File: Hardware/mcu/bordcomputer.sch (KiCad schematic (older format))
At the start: 4 parts, among them P101 CONN_1, P102 CONN_1, P103 CONN_1, P104 CONN_1

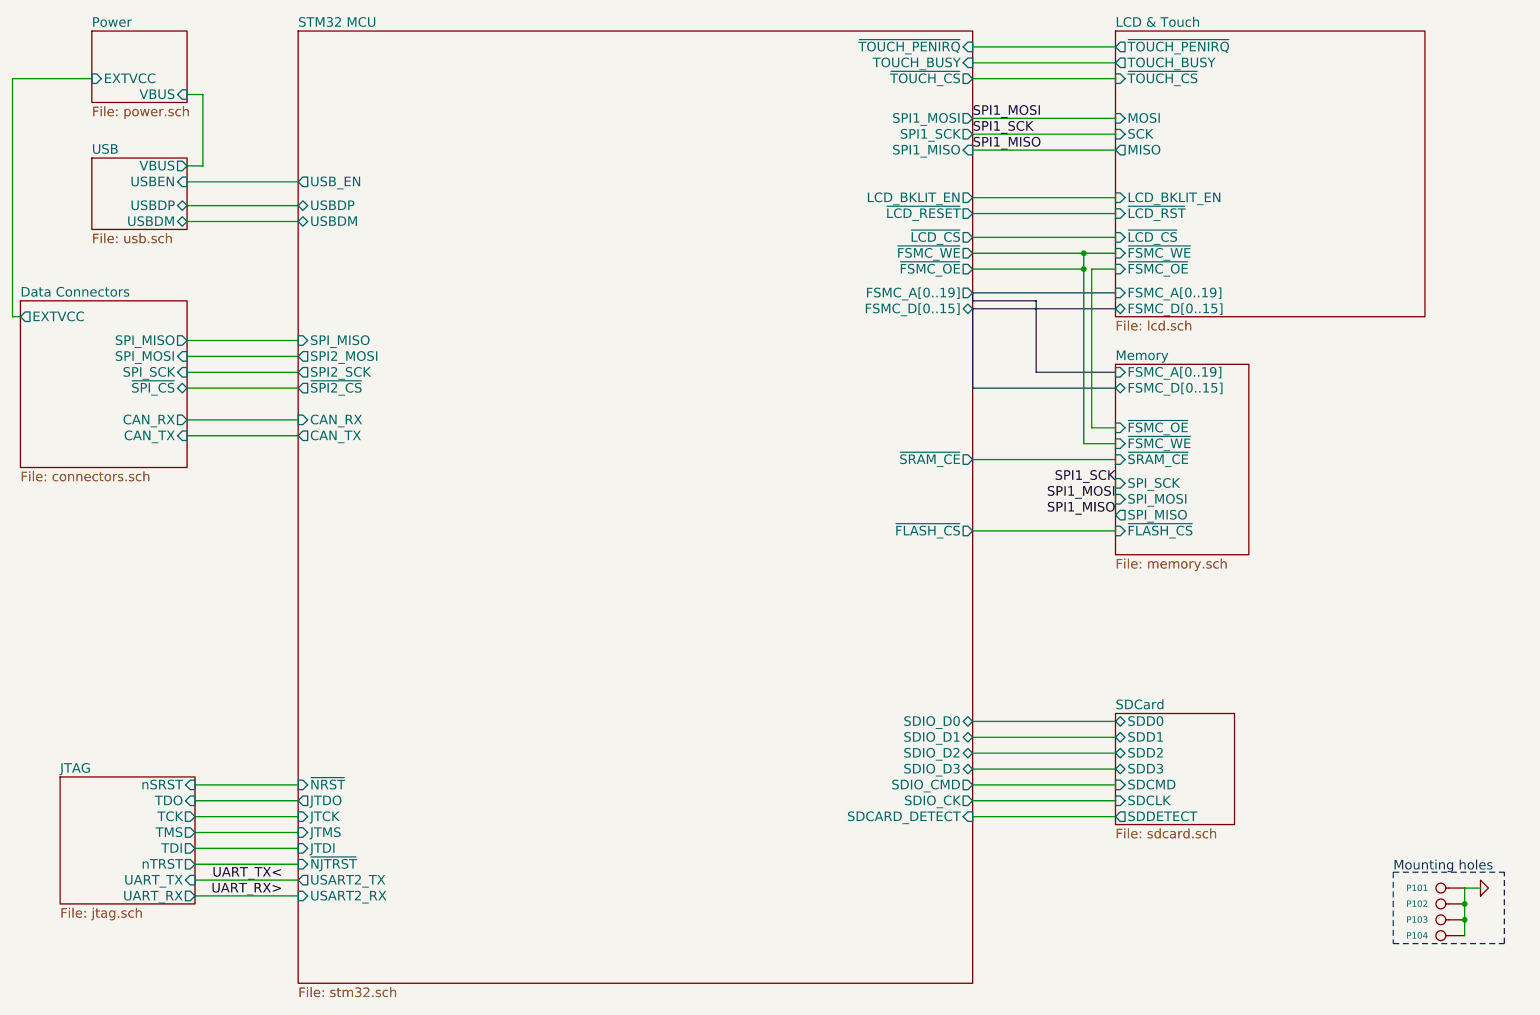
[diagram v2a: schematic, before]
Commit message: using adc instead of analog multiplexer for sensor board, some work on mcu board
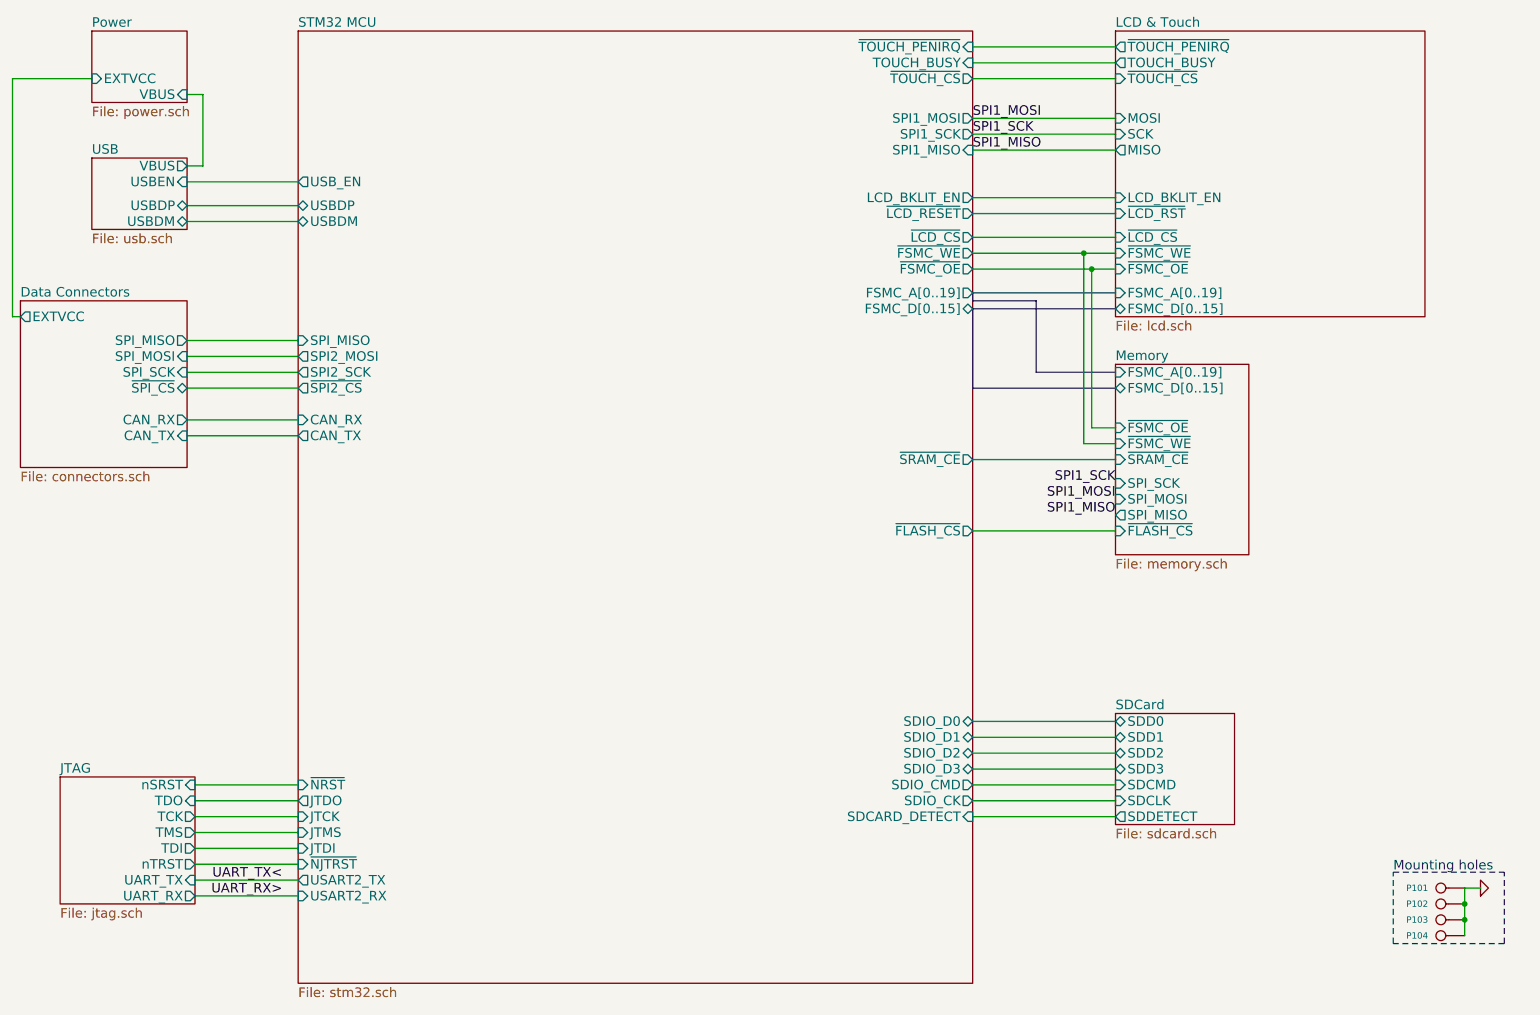
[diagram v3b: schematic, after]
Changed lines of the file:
@@
-EESchema Schematic File Version 2  date Mo 21 Mär 2011 03:16:23 CET
+EESchema Schematic File Version 2  date Di 17 Mai 2011 02:16:23 CEST
 LIBS:power
 LIBS:device
@@
 Sheet 1 9
 Title ""
-Date "21 mar 2011"
+Date "17 may 2011"
 Rev ""
 Comp ""
@@
 Comment4 ""
 $EndDescr
-Wire Notes Line
-	9850 6500 10550 6500
-Wire Notes Line
-	9850 6500 9850 6950
-Wire Notes Line
-	9850 6950 10550 6950
-Wire Notes Line
-	10550 6950 10550 6500
-Connection ~ 10300 6700
+Connection ~ 7950 2700
 Wire Wire Line
-	10400 6600 10300 6600
+	7200 2700 8100 2700
+Connection ~ 10300 6800
+Wire Wire Line
+	10300 6900 10300 6600
+Wire Wire Line
+	8100 4350 7200 4350
+Wire Wire Line
+	2950 3750 2250 3750
+Wire Wire Line
+	1650 1500 1150 1500
+Wire Wire Line
+	1150 1500 1150 3000
+Wire Wire Line
+	1150 3000 1200 3000
+Wire Bus Line
+	7600 2900 7600 3350
+Wire Bus Line
+	7600 2900 7200 2900
+Wire Bus Line
+	7200 2900 7200 2850
+Wire Bus Line
+	8100 2950 7200 2950
+Wire Bus Line
+	7600 3350 8100 3350
+Wire Wire Line
+	7200 1500 8100 1500
+Wire Wire Line
+	7200 1400 8100 1400
+Wire Wire Line
+	7200 1300 8100 1300
+Wire Wire Line
+	2300 6650 2950 6650
+Wire Wire Line
+	2300 6550 2950 6550
+Wire Wire Line
+	2300 6450 2950 6450
+Wire Wire Line
+	2300 6350 2950 6350
+Wire Wire Line
+	2300 6250 2950 6250
+Wire Wire Line
+	2300 6150 2950 6150
+Wire Wire Line
+	2300 6050 2950 6050
+Wire Wire Line
+	2300 5950 2950 5950
+Wire Wire Line
+	2950 2400 2250 2400
+Wire Wire Line
+	2950 2300 2250 2300
+Wire Wire Line
+	7200 3900 8100 3900
+Connection ~ 7900 2600
+Wire Wire Line
+	7200 2600 8100 2600
+Wire Wire Line
+	8100 3800 7900 3800
+Wire Wire Line
+	7900 3800 7900 2600
+Wire Wire Line
+	2250 2050 2350 2050
+Wire Wire Line
+	2350 2050 2350 1600
+Wire Wire Line
+	2350 1600 2250 1600
+Wire Wire Line
+	7950 2700 7950 3700
+Wire Wire Line
+	7950 3700 8100 3700
+Wire Wire Line
+	7200 2500 8100 2500
+Wire Bus Line
+	7200 2850 8100 2850
+Wire Wire Line
+	2250 2150 2950 2150
+Wire Wire Line
+	8100 5550 7200 5550
+Wire Wire Line
+	8100 5650 7200 5650
+Wire Wire Line
+	8100 5750 7200 5750
+Wire Wire Line
+	8100 5850 7200 5850
+Wire Wire Line
+	8100 5950 7200 5950
+Wire Wire Line
+	8100 6050 7200 6050
+Wire Wire Line
+	8100 6150 7200 6150
+Wire Wire Line
+	7200 2250 8100 2250
+Wire Wire Line
+	7200 2350 8100 2350
+Wire Bus Line
+	7200 2950 7200 3450
+Wire Bus Line
+	7200 3450 8100 3450
+Wire Wire Line
+	7200 1750 8100 1750
+Wire Wire Line
+	7200 1850 8100 1850
+Wire Wire Line
+	7200 1950 8100 1950
+Wire Wire Line
+	2250 3650 2950 3650
+Wire Wire Line
+	2250 3150 2950 3150
+Wire Wire Line
+	2250 3250 2950 3250
+Wire Wire Line
+	2250 3350 2950 3350
 Wire Wire Line
 	2250 3450 2950 3450
 Wire Wire Line
-	2250 3350 2950 3350
-Wire Wire Line
-	2250 3250 2950 3250
-Wire Wire Line
-	2250 3150 2950 3150
-Wire Wire Line
-	2250 3650 2950 3650
-Wire Wire Line
-	7200 1950 8100 1950
-Wire Wire Line
-	7200 1850 8100 1850
-Wire Wire Line
-	7200 1750 8100 1750
-Wire Bus Line
-	8100 3450 7200 3450
-Wire Bus Line
-	7200 3450 7200 2950
-Wire Wire Line
-	7200 2350 8100 2350
-Wire Wire Line
-	7200 2250 8100 2250
-Wire Wire Line
-	8100 6150 7200 6150
-Wire Wire Line
-	8100 6050 7200 6050
-Wire Wire Line
-	8100 5950 7200 5950
-Wire Wire Line
-	8100 5850 7200 5850
-Wire Wire Line
-	8100 5750 7200 5750
-Wire Wire Line
-	8100 5650 7200 5650
-Wire Wire Line
-	8100 5550 7200 5550
-Wire Wire Line
-	2250 2150 2950 2150
-Wire Bus Line
-	8100 2850 7200 2850
-Connection ~ 7900 2700
-Wire Wire Line
-	7200 2700 7900 2700
-Wire Wire Line
-	7200 2500 8100 2500
-Wire Wire Line
-	8100 3700 7950 3700
-Wire Wire Line
-	7950 3700 7950 2700
-Wire Wire Line
-	7950 2700 8100 2700
-Wire Wire Line
-	2250 1600 2350 1600
-Wire Wire Line
-	2350 1600 2350 2050
-Wire Wire Line
-	2350 2050 2250 2050
-Wire Wire Line
-	7900 2600 7900 3800
-Wire Wire Line
-	7900 3800 8100 3800
-Wire Wire Line
-	7200 2600 8100 2600
-Connection ~ 7900 2600
-Wire Wire Line
-	7200 3900 8100 3900
-Wire Wire Line
-	2950 2300 2250 2300
-Wire Wire Line
-	2950 2400 2250 2400
-Wire Wire Line
-	2300 5950 2950 5950
-Wire Wire Line
-	2300 6050 2950 6050
-Wire Wire Line
-	2300 6150 2950 6150
-Wire Wire Line
-	2300 6250 2950 6250
-Wire Wire Line
-	2300 6350 2950 6350
-Wire Wire Line
-	2300 6450 2950 6450
-Wire Wire Line
-	2300 6550 2950 6550
-Wire Wire Line
-	2300 6650 2950 6650
-Wire Wire Line
-	7200 1300 8100 1300
-Wire Wire Line
-	7200 1400 8100 1400
-Wire Wire Line
-	7200 1500 8100 1500
-Wire Bus Line
-	8100 3350 7600 3350
-Wire Bus Line
-	7200 2950 8100 2950
-Wire Bus Line
-	7200 2850 7200 2900
-Wire Bus Line
-	7200 2900 7600 2900
-Wire Bus Line
-	7600 2900 7600 3350
-Wire Wire Line
-	1200 3000 1150 3000
-Wire Wire Line
-	1150 3000 1150 1500
-Wire Wire Line
-	1150 1500 1650 1500
-Wire Wire Line
-	2950 3750 2250 3750
-Wire Wire Line
-	8100 4350 7200 4350
-Wire Wire Line
-	10300 6600 10300 6900
-Connection ~ 10300 6800
+	10300 6600 10400 6600
+Connection ~ 10300 6700
+Wire Notes Line
+	10550 6950 10550 6500
+Wire Notes Line
+	10550 6950 9850 6950
+Wire Notes Line
+	9850 6950 9850 6500
+Wire Notes Line
+	9850 6500 10550 6500
 $Comp
 L GND #PWR01
